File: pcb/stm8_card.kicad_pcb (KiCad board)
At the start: 2 copper layers, 101.6 x 50.8 mm, 22 parts, among them J1 DEBUG HEADER, SW1 TL59AF100Q, SW2 TL59AF100Q, SW3 TL59AF100Q, SW4 TL3302AF260QG, U1 ER-OLED0.91-7, U2 STM8S103F3

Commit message: pcb small edits
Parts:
- moved C8 162.5 mm to (167.6, 149.9)
- moved C6 152.0 mm to (167.6, 139.7)
- moved C4 151.2 mm to (167.6, 127.0)
- moved R4 126.7 mm to (149.9, 105.4)
- moved R3 124.7 mm to (149.9, 101.6)
- moved C7 89.2 mm to (167.6, 144.8)
- moved C5 86.4 mm to (167.6, 133.3)
- moved R2 61.3 mm to (149.9, 97.8)
- moved C3 58.6 mm to (167.6, 121.9)
- moved R1 57.3 mm to (149.9, 92.7)
- moved C1 54.7 mm to (166.6, 111.8)
- moved R5 44.6 mm to (149.9, 111.8)
- moved C2 39.0 mm to (167.4, 116.8), turned to 180 degrees
- moved R6 32.4 mm to (149.9, 116.8)
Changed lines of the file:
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@@
   )
   (module Capacitor_SMD:C_0805_2012Metric_Pad1.18x1.45mm_HandSolder (layer F.Cu)
-    (at 114.115001 127.205001)
+    (at 166.6025 111.76)
     (descr "Capacitor SMD 0805 (2012 Metric), square (rectangular) end terminal, IPC_7351 nominal with elongated pad for handsoldering. (Body size source: IPC-SM-782 page 76, https://www.pcb-3d.com/wordpress/wp-content/uploads/ipc-sm-782a_amendment_1_and_2.pdf, https://docs.google.com/spreadsheets/d/1BsfQQcO9C6DZCsRaXUlFlo91Tg2WpOkGARC1WS5S8t0/edit?usp=sharing), generated with kicad-footprint-generator")
     (tags "capacitor handsolder")
@@
   )
   (module Capacitor_SMD:C_0805_2012Metric_Pad1.18x1.45mm_HandSolder (layer F.Cu)
-    (at 128.545001 114.035001)
+    (at 167.4075 116.84 180)
     (descr "Capacitor SMD 0805 (2012 Metric), square (rectangular) end terminal, IPC_7351 nominal with elongated pad for handsoldering. (Body size source: IPC-SM-782 page 76, https://www.pcb-3d.com/wordpress/wp-content/uploads/ipc-sm-782a_amendment_1_and_2.pdf, https://docs.google.com/spreadsheets/d/1BsfQQcO9C6DZCsRaXUlFlo91Tg2WpOkGARC1WS5S8t0/edit?usp=sharing), generated with kicad-footprint-generator")
     (tags "capacitor handsolder")
@@
       (effects (font (size 0.5 0.5) (thickness 0.08)))
     )
-    (pad 1 smd roundrect (at -1.0375 0) (size 1.175 1.45) (layers F.Cu F.Paste F.Mask) (roundrect_rratio 0.212766)
+    (pad 1 smd roundrect (at -1.0375 0 180) (size 1.175 1.45) (layers F.Cu F.Paste F.Mask) (roundrect_rratio 0.212766)
       (net 5 "Net-(C2-Pad1)"))
-    (pad 2 smd roundrect (at 1.0375 0) (size 1.175 1.45) (layers F.Cu F.Paste F.Mask) (roundrect_rratio 0.212766)
+    (pad 2 smd roundrect (at 1.0375 0 180) (size 1.175 1.45) (layers F.Cu F.Paste F.Mask) (roundrect_rratio 0.212766)
       (net 6 "Net-(C2-Pad2)"))
     (model ${KISYS3DMOD}/Capacitor_SMD.3dshapes/C_0805_2012Metric.wrl
@@
   )
   (module Capacitor_SMD:C_0805_2012Metric_Pad1.18x1.45mm_HandSolder (layer F.Cu)
-    (at 109.305001 127.205001)
+    (at 167.64 121.92)
     (descr "Capacitor SMD 0805 (2012 Metric), square (rectangular) end terminal, IPC_7351 nominal with elongated pad for handsoldering. (Body size source: IPC-SM-782 page 76, https://www.pcb-3d.com/wordpress/wp-content/uploads/ipc-sm-782a_amendment_1_and_2.pdf, https://docs.google.com/spreadsheets/d/1BsfQQcO9C6DZCsRaXUlFlo91Tg2WpOkGARC1WS5S8t0/edit?usp=sharing), generated with kicad-footprint-generator")
     (tags "capacitor handsolder")
@@
   )
   (module Capacitor_SMD:C_0805_2012Metric_Pad1.18x1.45mm_HandSolder (layer F.Cu)
-    (at 27.015001 71.515001)
+    (at 167.64 127)
     (descr "Capacitor SMD 0805 (2012 Metric), square (rectangular) end terminal, IPC_7351 nominal with elongated pad for handsoldering. (Body size source: IPC-SM-782 page 76, https://www.pcb-3d.com/wordpress/wp-content/uploads/ipc-sm-782a_amendment_1_and_2.pdf, https://docs.google.com/spreadsheets/d/1BsfQQcO9C6DZCsRaXUlFlo91Tg2WpOkGARC1WS5S8t0/edit?usp=sharing), generated with kicad-footprint-generator")
     (tags "capacitor handsolder")
@@
     (fp_line (start -1 -0.625) (end 1 -0.625) (layer F.Fab) (width 0.1))
     (fp_line (start -1 0.625) (end -1 -0.625) (layer F.Fab) (width 0.1))
-    (fp_text user %R (at 0 0) (layer F.Fab)
+    (fp_text user %R (at 1 -0.625) (layer F.Fab)
       (effects (font (size 0.5 0.5) (thickness 0.08)))
     )
@@
   )
   (module Capacitor_SMD:C_0805_2012Metric_Pad1.18x1.45mm_HandSolder (layer F.Cu)
-    (at 83.665001 153.825001)
+    (at 167.64 133.35)
     (descr "Capacitor SMD 0805 (2012 Metric), square (rectangular) end terminal, IPC_7351 nominal with elongated pad for handsoldering. (Body size source: IPC-SM-782 page 76, https://www.pcb-3d.com/wordpress/wp-content/uploads/ipc-sm-782a_amendment_1_and_2.pdf, https://docs.google.com/spreadsheets/d/1BsfQQcO9C6DZCsRaXUlFlo91Tg2WpOkGARC1WS5S8t0/edit?usp=sharing), generated with kicad-footprint-generator")
     (tags "capacitor handsolder")
@@
   )
   (module Capacitor_SMD:C_0805_2012Metric_Pad1.18x1.45mm_HandSolder (layer F.Cu)
-    (at 31.825001 71.505001)
+    (at 167.64 139.7)
     (descr "Capacitor SMD 0805 (2012 Metric), square (rectangular) end terminal, IPC_7351 nominal with elongated pad for handsoldering. (Body size source: IPC-SM-782 page 76, https://www.pcb-3d.com/wordpress/wp-content/uploads/ipc-sm-782a_amendment_1_and_2.pdf, https://docs.google.com/spreadsheets/d/1BsfQQcO9C6DZCsRaXUlFlo91Tg2WpOkGARC1WS5S8t0/edit?usp=sharing), generated with kicad-footprint-generator")
     (tags "capacitor handsolder")
@@
   )
   (module Capacitor_SMD:C_0805_2012Metric_Pad1.18x1.45mm_HandSolder (layer F.Cu)
-    (at 78.855001 153.825001)
+    (at 167.64 144.78)
     (descr "Capacitor SMD 0805 (2012 Metric), square (rectangular) end terminal, IPC_7351 nominal with elongated pad for handsoldering. (Body size source: IPC-SM-782 page 76, https://www.pcb-3d.com/wordpress/wp-content/uploads/ipc-sm-782a_amendment_1_and_2.pdf, https://docs.google.com/spreadsheets/d/1BsfQQcO9C6DZCsRaXUlFlo91Tg2WpOkGARC1WS5S8t0/edit?usp=sharing), generated with kicad-footprint-generator")
     (tags "capacitor handsolder")
@@
   )
   (module Capacitor_SMD:C_0805_2012Metric_Pad1.18x1.45mm_HandSolder (layer F.Cu)
-    (at 27.015001 68.505001)
+    (at 167.64 149.86)
     (descr "Capacitor SMD 0805 (2012 Metric), square (rectangular) end terminal, IPC_7351 nominal with elongated pad for handsoldering. (Body size source: IPC-SM-782 page 76, https://www.pcb-3d.com/wordpress/wp-content/uploads/ipc-sm-782a_amendment_1_and_2.pdf, https://docs.google.com/spreadsheets/d/1BsfQQcO9C6DZCsRaXUlFlo91Tg2WpOkGARC1WS5S8t0/edit?usp=sharing), generated with kicad-footprint-generator")
     (tags "capacitor handsolder")
@@
   )
   (module Resistor_SMD:R_0805_2012Metric_Pad1.20x1.40mm_HandSolder (layer F.Cu)
-    (at 109.275001 133.135001)
+    (at 149.86 92.71)
     (descr "Resistor SMD 0805 (2012 Metric), square (rectangular) end terminal, IPC_7351 nominal with elongated pad for handsoldering. (Body size source: IPC-SM-782 page 72, https://www.pcb-3d.com/wordpress/wp-content/uploads/ipc-sm-782a_amendment_1_and_2.pdf), generated with kicad-footprint-generator")
     (tags "resistor handsolder")
@@
   )
   (module Resistor_SMD:R_0805_2012Metric_Pad1.20x1.40mm_HandSolder (layer F.Cu)
-    (at 104.065001 138.555001)
+    (at 149.86 97.79)
     (descr "Resistor SMD 0805 (2012 Metric), square (rectangular) end terminal, IPC_7351 nominal with elongated pad for handsoldering. (Body size source: IPC-SM-782 page 72, https://www.pcb-3d.com/wordpress/wp-content/uploads/ipc-sm-782a_amendment_1_and_2.pdf), generated with kicad-footprint-generator")
     (tags "resistor handsolder")
@@
   )
   (module Resistor_SMD:R_0805_2012Metric_Pad1.20x1.40mm_HandSolder (layer F.Cu)
-    (at 27.485001 77.445001)
+    (at 149.86 101.575001)
     (descr "Resistor SMD 0805 (2012 Metric), square (rectangular) end terminal, IPC_7351 nominal with elongated pad for handsoldering. (Body size source: IPC-SM-782 page 72, https://www.pcb-3d.com/wordpress/wp-content/uploads/ipc-sm-782a_amendment_1_and_2.pdf), generated with kicad-footprint-generator")
     (tags "resistor handsolder")
@@
   )
   (module Resistor_SMD:R_0805_2012Metric_Pad1.20x1.40mm_HandSolder (layer F.Cu)
-    (at 26.985001 74.495001)
+    (at 149.86 105.41)
     (descr "Resistor SMD 0805 (2012 Metric), square (rectangular) end terminal, IPC_7351 nominal with elongated pad for handsoldering. (Body size source: IPC-SM-782 page 72, https://www.pcb-3d.com/wordpress/wp-content/uploads/ipc-sm-782a_amendment_1_and_2.pdf), generated with kicad-footprint-generator")
     (tags "resistor handsolder")
@@
   )
   (module Resistor_SMD:R_0805_2012Metric_Pad1.20x1.40mm_HandSolder (layer F.Cu)
-    (at 109.275001 130.185001)
+    (at 149.86 111.76)
     (descr "Resistor SMD 0805 (2012 Metric), square (rectangular) end terminal, IPC_7351 nominal with elongated pad for handsoldering. (Body size source: IPC-SM-782 page 72, https://www.pcb-3d.com/wordpress/wp-content/uploads/ipc-sm-782a_amendment_1_and_2.pdf), generated with kicad-footprint-generator")
     (tags "resistor handsolder")
@@
   )
   (module Resistor_SMD:R_0805_2012Metric_Pad1.20x1.40mm_HandSolder (layer F.Cu)
-    (at 118.025001 123.125001)
-    (descr "Resistor SMD 0805 (2012 Metric), square (rectangular) end terminal, IPC_7351 nominal with elongated pad for handsoldering. (Body size source: IPC-SM-782 page 72, https://www.pcb-3d.com/wordpress/wp-content/uploads/ipc-sm-782a_amendment_1_and_2.pdf), generated with kicad-footprint-generator")
-    (tags "resistor handsolder")
+    (at 149.86 116.84)
+    (descr "Resistor SMD 0805 (2012 Metric), square (rectangular) end terminal, IPC_7351 nominal with elongated pad for handsoldering. (Body size source: IPC-SM-782 page 72, https://www.pcb-3d.com/wordpress/wp-content/uploads/ipc-sm-782a_amendment_1_and_2.pdf), generated with kicad-footprint-generator")
+    (tags "resistor handsolder")

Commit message: pcbupdates
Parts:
- BT1: footprint Battery:BatteryHolder_Keystone_103_1x20mm -> stm8_card:BatteryHolder_Keystone_103_1x20mm_Corrected
- moved R6 111.6 mm to (261.0, 107.0), turned to 270 degrees
- moved R5 108.7 mm to (258.5, 107.0), turned to 270 degrees
- moved R4 106.2 mm to (256.0, 107.0), turned to 90 degrees
- moved C8 105.0 mm to (263.5, 107.0), turned to 90 degrees
- moved R3 103.8 mm to (253.5, 107.0), turned to 90 degrees
- moved R2 101.1 mm to (250.5, 107.0), turned to 90 degrees
- moved C1 81.5 mm to (248.0, 107.0), turned to 90 degrees
- moved R1 78.5 mm to (227.0, 107.0), turned to 90 degrees
- moved C2 78.2 mm to (245.0, 107.0), turned to 90 degrees
- moved C3 75.8 mm to (242.0, 107.0), turned to 90 degrees
- moved C4 74.1 mm to (239.0, 107.0), turned to 90 degrees
- moved C5 73.2 mm to (236.0, 107.0), turned to 270 degrees
- moved C6 73.1 mm to (233.0, 107.0), turned to 270 degrees
- moved C7 72.9 mm to (230.0, 107.0), turned to 270 degrees
- moved SW4 28.1 mm to (247.0, 148.6), turned to 180 degrees
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
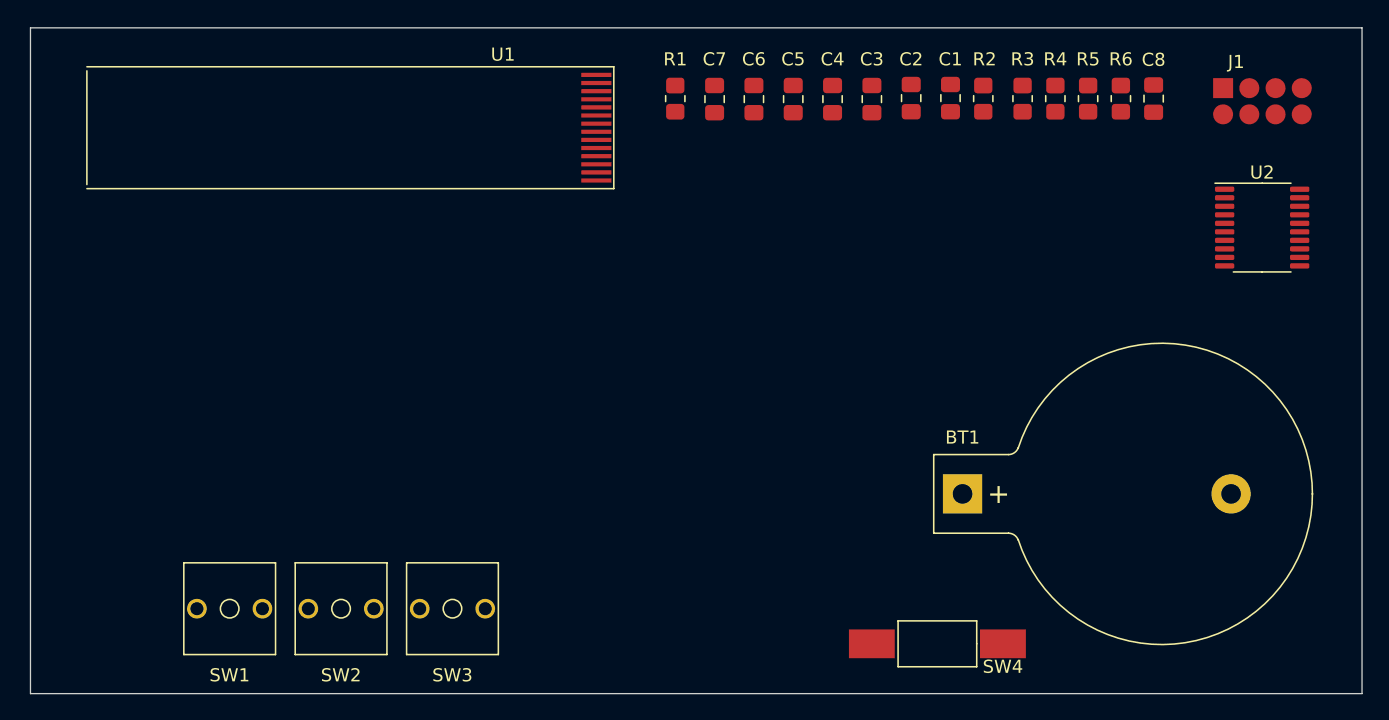
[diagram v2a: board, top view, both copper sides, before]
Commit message: updated dimensions
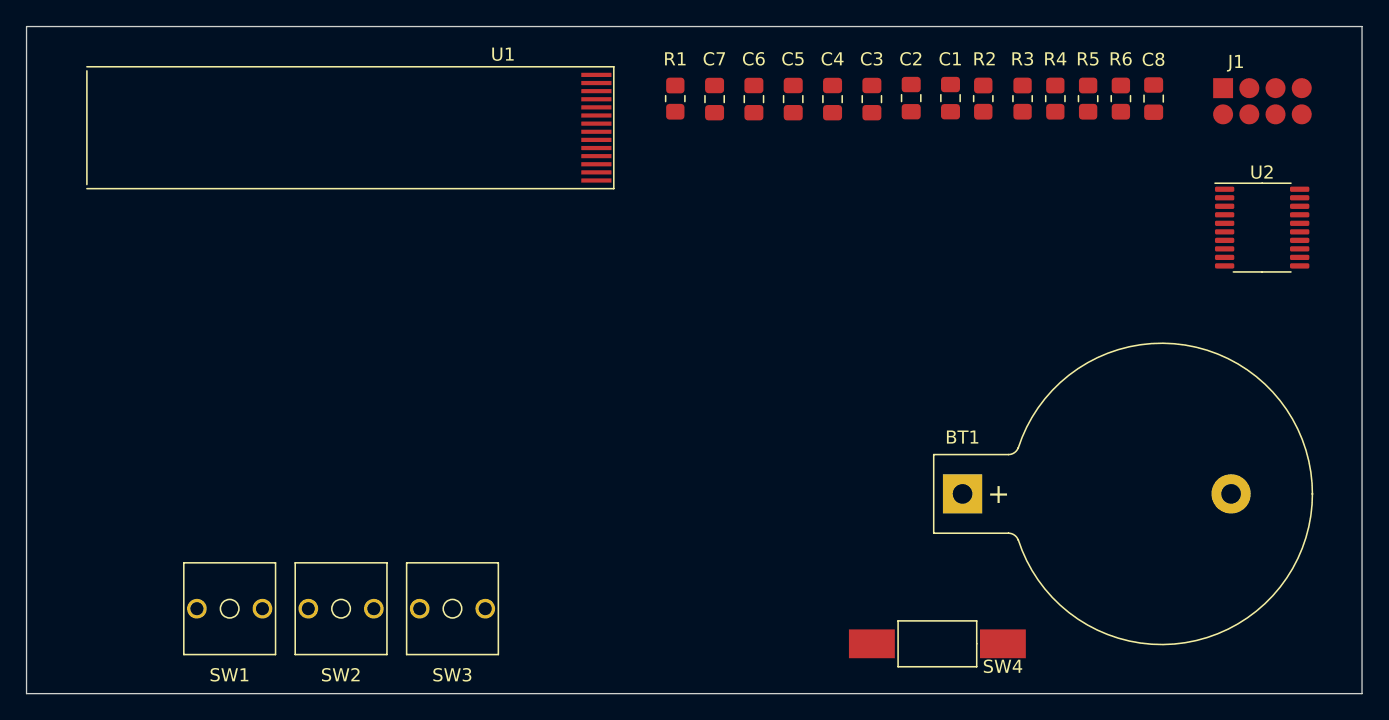
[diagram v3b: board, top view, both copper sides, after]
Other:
- board size 101.6 x 50.8 mm -> 101.9 x 50.9 mm
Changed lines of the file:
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@@
   (general
     (thickness 1.6)
-    (drawings 4)
+    (drawings 6)
     (tracks 0)
     (zones 0)
@@
     )
   )
-  (gr_line (start 279.4 101.6) (end 177.8 101.6) (layer Edge.Cuts) (width 0.05))
-  (gr_line (start 279.4 152.4) (end 279.4 101.6) (layer Edge.Cuts) (width 0.05))
-  (gr_line (start 177.8 152.4) (end 279.4 152.4) (layer Edge.Cuts) (width 0.05))
-  (gr_line (start 177.8 101.6) (end 177.8 152.4) (layer Edge.Cuts) (width 0.05))
+  (dimension 51 (width 0.15) (layer Dwgs.User)
+    (gr_text "51.000 mm" (at 168.2 127 90) (layer Dwgs.User)
+      (effects (font (size 1 1) (thickness 0.15)))
+    )
+    (feature1 (pts (xy 173 101.5) (xy 168.913579 101.5)))
+    (feature2 (pts (xy 173 152.5) (xy 168.913579 152.5)))
+    (crossbar (pts (xy 169.5 152.5) (xy 169.5 101.5)))
+    (arrow1a (pts (xy 169.5 101.5) (xy 170.086421 102.626504)))
+    (arrow1b (pts (xy 169.5 101.5) (xy 168.913579 102.626504)))
+    (arrow2a (pts (xy 169.5 152.5) (xy 170.086421 151.373496)))
+    (arrow2b (pts (xy 169.5 152.5) (xy 168.913579 151.373496)))
+  )
+  (dimension 102 (width 0.15) (layer Dwgs.User)
+    (gr_text "102.000 mm" (at 228.5 82.7) (layer Dwgs.User)
+      (effects (font (size 1 1) (thickness 0.15)))
+    )
+    (feature1 (pts (xy 279.5 96.5) (xy 279.5 83.413579)))
+    (feature2 (pts (xy 177.5 96.5) (xy 177.5 83.413579)))
+    (crossbar (pts (xy 177.5 84) (xy 279.5 84)))
+    (arrow1a (pts (xy 279.5 84) (xy 278.373496 84.586421)))
+    (arrow1b (pts (xy 279.5 84) (xy 278.373496 83.413579)))
+    (arrow2a (pts (xy 177.5 84) (xy 178.626504 84.586421)))
+    (arrow2b (pts (xy 177.5 84) (xy 178.626504 83.413579)))
+  )
+  (gr_line (start 279.4 101.5) (end 177.5 101.5) (layer Edge.Cuts) (width 0.05))
+  (gr_line (start 279.4 152.4) (end 279.4 101.5) (layer Edge.Cuts) (width 0.05))
+  (gr_line (start 177.5 152.4) (end 279.4 152.4) (layer Edge.Cuts) (width 0.05))
+  (gr_line (start 177.5 101.5) (end 177.5 152.4) (layer Edge.Cuts) (width 0.05))
 )
